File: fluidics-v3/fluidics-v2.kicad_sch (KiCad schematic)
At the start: 41 parts, among them J1 PJ-063AH, J10 87832-0410, J11 0705430001, J12 87832-0410, J13 0705430001, J14 87832-0410, J15 0533980671, J16 0705430001, J17 0533980671, J18 87832-0410, J19 0705430001, J2 B6B-ZR-SM4-TF, J20 0533980671, J21 87832-0410, J22 0705430001, J24 0705430001, J25 87832-0410, J3 A-DS_15_A_KG-T4S, J4 B6B-ZR-SM4-TF, J6 SSM-124-L-SV, J7 SSM-124-L-SV, U2 Teensy4.1

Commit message: U4: replace Pololu D24V10FX with Traco TSR1-2450E, drop 5V power-good
Swap the 24V->5V step-down for a Traco TSR 1-2450E (SIP-3, through-hole,
1A) using the stock KiCad symbol/footprint pair. The TSR is a 3-pin part,
so the Pololu's PG and nSHDN pins go away; nSHDN was already unconnected.

Schematic:
- psu: U4 -> Converter_DCDC:TSR1-2450E on
  Converter_DCDC:Converter_DCDC_TRACO_TSR1-xxxxE_THT
- Remove the PG-5V hierarchical label, sheet pin, wire stub and the 47k
  pull-up R51; PG-5V no longer exists as a net
- No-connect flags on J7 pin 1 and U2 pin 25, freeing Teensy pin 33

PCB:
- Place U4 at (156.437, 71.905) rot +90 so Vin lands on the existing +24V
  arrival node; GND and Vout follow on the 2.54mm pitch. Rotating rather
  than mirroring keeps the TSR body clear of R3 and D2, which the part
  would otherwise sit on top of.
- Route +5V on F.Cu 0.55mm from the existing tap across to Vout, plus a
  via restoring the F.Cu/B.Cu junction the old through-hole pad provided
- Remove orphaned PG-5V copper (16 segments, 2 vias) and the now-dead
  6-segment +3.3V run that used to feed R51

DRC: 0 errors, schematic parity clean, unconnected 7 -> 6.
Courtyard overlaps 2 -> 0, dangling tracks 4 -> 0. ERC 33 -> 31.
One cosmetic silkscreen warning remains: the "24V->5V Module" board label
now overlaps U4's outline and wants nudging by hand.

Co-Authored-By: Claude Opus 5 (1M context) <noreply@anthropic.com>
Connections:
- net PG-5V: no longer names the net of U2.25 (33_MCLK2)
- net PG-5V: no longer J7.1 (Pin_1)
- no-connect marks 51 -> 53
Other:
- sheet Power Supplies ports: added none; removed PG-5V
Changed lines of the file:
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@@
 	)
 	(no_connect
+		(at 60.96 271.78)
+	)
+	(no_connect
+		(at 284.48 251.46)
+	)
+	(no_connect
 		(at 101.6 248.92)
 	)
@@
 	(wire
 		(pts
-			(xy 116.84 154.94) (xy 128.27 154.94)
-		)
-		(stroke
-			(width 0)
-			(type default)
-		)
-	)
-	(wire
-		(pts
 			(xy 303.53 210.82) (xy 303.53 205.74)
 		)
@@
 		)
 	)
-	(label "PG-5V"
-		(at 119.38 154.94 0)
-		(effects
-			(font
-				(size 1.27 1.27)
-			)
-			(justify left bottom)
-		)
-	)
 	(label "GPIO_9"
 		(at 228.6 205.74 180)
@@
 		)
 	)
-	(label "PG-5V"
-		(at 284.48 251.46 0)
-		(effects
-			(font
-				(size 1.27 1.27)
-			)
-			(justify left bottom)
-		)
-	)
 	(label "~{CS}3"
 		(at 285.75 248.92 0)
@@
 		)
 	)
-	(label "PG-5V"
-		(at 60.96 271.78 0)
-		(effects
-			(font
-				(size 1.27 1.27)
-			)
-			(justify left bottom)
-		)
-	)
 	(label "PG-12V"
 		(at 228.6 251.46 180)
@@
 			)
 		)
-		(pin "PG-5V" output
-			(at 116.84 154.94 0)
-			(effects
-				(font
-					(size 1.27 1.27)
-				)
-				(justify right)
-			)
-		)

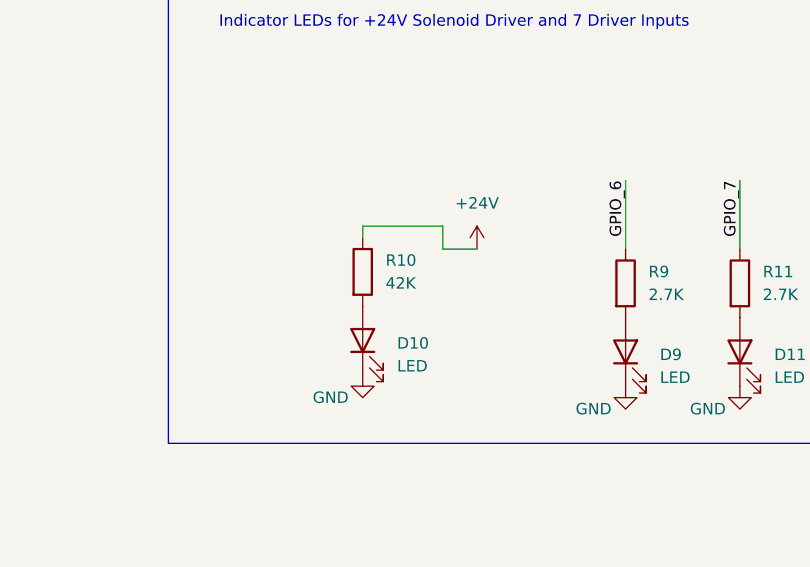
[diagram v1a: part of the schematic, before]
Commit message: v3: finish TSR regulator swap, reconcile BOM, regenerate fab outputs
Follow-up to a773dae, which replaced the Pololu D24V10FX with a Traco
TSR 1-2450E. Completes the board cleanup and brings the fabrication
package back in step with the design.

Board:
- Remove the redundant B.Cu 3.3V spine at x=152.62; the 3V3_bridge_Bcu
  zone already carried that path, so connectivity is unchanged
- Move the "24V->5V Module" silk label clear of U4's outline
- R10 42K -> 47K. 42k is not an E24 value; R4 already uses 47k on the
  same +24V rail feeding an identical indicator LED, and the current
  difference is 0.52mA vs 0.47mA

DRC 0 errors, schematic parity clean, 6 unconnected items (all
pre-existing). Courtyard overlaps and dangling tracks both at 0.

Fabrication outputs, all regenerated from the current board:
- gerbers/ + drill (4-layer, metric 4.6, X2, merged PTH/NPTH), rezipped
- positions.csv, netlist.ipc, fluidics-v3.step

BOM and CPL:
- Add fluidics-v3-bom.xlsx, flattened from the EasyEDA template that
  broke JLC's importer: header moved to row 1, dropping five preamble
  rows, merged cells A1:D5, an embedded logo, =ROW() formulas whose
  cached values were lost on re-save, and four phantom trailing rows.
  Supplier Part renamed to "LCSC Part #" for auto-detection.
- Reconcile it against the board: add U4 (TSR 1-2450E, C5346721), drop
  R51 from the R10,R51 group (the PG pull-up died with the power-good
  net), correct U3 to AP2112K-3.3TRG1 / C51118 (was still the
  AP7366EA-33W5-7 part number from before 864ac36)
- Add cpl_jlcpcb.csv in JLCPCB column format
- Remove bom.csv: superseded, no LCSC column, and its range notation
  (C15-C17, R39-R44) is unparseable by JLC

BOM and CPL now agree exactly: 74 designators, 74 rows, no mismatch in
either direction, every line carrying an LCSC part number.

Co-Authored-By: Claude Opus 5 (1M context) <noreply@anthropic.com>
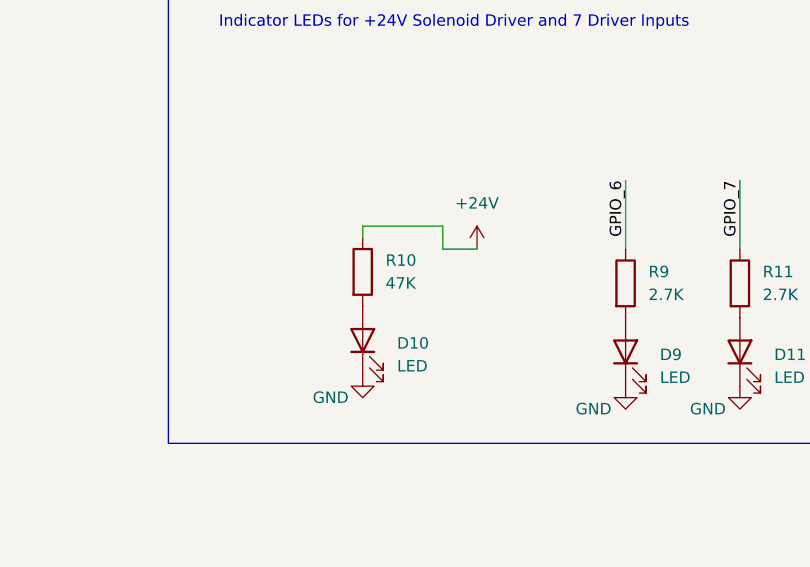
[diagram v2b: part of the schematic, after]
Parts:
- R10: value 42K -> 47K
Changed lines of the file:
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@@
 	)
 	(no_connect
-		(at 60.96 271.78)
-	)
-	(no_connect
-		(at 284.48 251.46)
-	)
-	(no_connect
 		(at 101.6 248.92)
 	)
@@
 	)
 	(no_connect
+		(at 60.96 271.78)
+	)
+	(no_connect
 		(at 240.03 92.71)
 	)
@@
 	)
 	(no_connect
+		(at 284.48 251.46)
+	)
+	(no_connect
 		(at 147.32 238.76)
 	)
@@
 			)
 		)
-		(property "Value" "42K"
+		(property "Value" "47K"
 			(at 120.65 74.9299 0)
 			(show_name no)
